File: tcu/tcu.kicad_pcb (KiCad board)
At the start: 2 copper layers, 52 parts, among them CON1 USB-MICRO-B, K1 SPDT_RELAY, K2 SPDT_RELAY, K3 SPDT_RELAY, P1 CONN_01X08, P2 CONN_02X03, P3 NRF24L01+, P4 ESP8266, Q1 E_NMOS, Q2 E_NMOS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

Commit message: further work on layout
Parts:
- D10: moved to B.Cu
- moved D10 108.0 mm to (68.1, 74.1)
- moved Q4 105.7 mm to (70.7, 60.1)
- moved R13 101.9 mm to (71.9, 65.2), turned to 180 degrees
- moved P4 99.3 mm to (163.3, 105.9), turned to 180 degrees
- moved P3 97.5 mm to (163.6, 84.3), turned to 180 degrees
- moved BR1 84.3 mm to (104.1, 39.4)
- moved BR3 84.3 mm to (134.6, 39.4)
- moved D1 84.3 mm to (149.9, 39.4)
- moved D3 84.3 mm to (88.9, 39.4)
- moved D5 84.3 mm to (88.9, 52.1)
- moved D6 84.3 mm to (149.9, 52.1)
- moved K1 84.3 mm to (111.8, 44.5)
- moved K2 84.3 mm to (81.3, 44.5)
- moved K3 84.3 mm to (142.2, 44.5)
- moved Q2 84.3 mm to (88.9, 47.0)
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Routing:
- net GND: track 0.00 -> 346.9 mm
- net Net-(C1-Pad1): track 0.00 -> 128.1 mm
- net Net-(BR2-Pad1): track 0.00 -> 60.3 mm
- net Net-(BR3-Pad2): track 0.00 -> 56.1 mm
- net VCC: track 0.00 -> 55.8 mm, vias 0 -> 1
- net Net-(BR3-Pad1): track 0.00 -> 37.9 mm
- net Net-(BR1-Pad1): track 0.00 -> 32.8 mm
- net Net-(BR1-Pad2): track 0.00 -> 30.7 mm
- net /MOSI: track 0.00 -> 18.2 mm, vias 0 -> 1
- net Net-(BR2-Pad2): track 18.9 -> 35.8 mm
- net Net-(D8-Pad2): track 0.00 -> 14.8 mm
- net /MISO: track 0.00 -> 9.08 mm
- net Net-(C4-Pad1): track 0.00 -> 8.67 mm
- net /SCK: track 0.00 -> 8.35 mm
- net Net-(C5-Pad1): track 0.00 -> 8.25 mm
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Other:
- net class power added: clearance 0.254, trace_width 0.6096, via_dia 0.889, via_drill 0.635

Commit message: squeezing in
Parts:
- moved F1 61.8 mm to (73.4, 75.2)
- moved CON1 60.8 mm to (77.0, 78.7)
- moved R1 60.8 mm to (77.0, 75.4)
- moved R2 60.8 mm to (78.7, 75.4)
- moved D7 58.4 mm to (75.4, 71.4), turned to 180 degrees
- moved P3 56.5 mm to (108.0, 74.2), turned to 0 degrees
- moved P4 52.7 mm to (116.6, 81.5), turned to 0 degrees
- moved C4 36.6 mm to (93.0, 64.8), turned to 90 degrees
- moved X1 35.7 mm to (96.3, 66.8), turned to 270 degrees
- moved U2 32.2 mm to (85.3, 66.5), turned to 90 degrees
- moved C6 31.4 mm to (76.5, 68.6), turned to 0 degrees
- moved C5 30.9 mm to (93.0, 69.1), turned to 270 degrees
- moved Q4 27.7 mm to (66.0, 87.4), turned to 180 degrees
- moved R10 23.4 mm to (93.0, 74.9), turned to 270 degrees
- moved R13 20.3 mm to (66.8, 84.8)
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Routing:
- net VCC: track 55.8 -> 177.4 mm, vias 1 -> 5
- net /RESET: track 6.77 -> 27.5 mm
- net GND: track 346.9 -> 361.2 mm, vias 0 -> 5
- net /D-: track 0.00 -> 10.9 mm, vias 0 -> 2
- net /D+: track 0.00 -> 9.58 mm, vias 0 -> 2
- net Net-(C1-Pad1): track 128.1 -> 119.7 mm
- net Net-(D10-Pad2): track 0.00 -> 7.50 mm, vias 0 -> 1
- net Net-(D10-Pad1): track 0.00 -> 2.70 mm, vias 0 -> 1
- net /MOSI: track 18.2 -> 20.0 mm, vias 1 -> 3
- net /UVCC: track 5.30 -> 7.02 mm
- net Net-(D7-Pad1): track 3.84 -> 5.42 mm
- net /SCK: track 8.35 -> 6.82 mm
- net /MISO: track 9.08 -> 7.55 mm
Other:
- net class Default: clearance 0.254 -> 0.1778
- net class power: clearance 0.254 -> 0.1778
- rule trace_clearance: 0.254 -> 0.1778

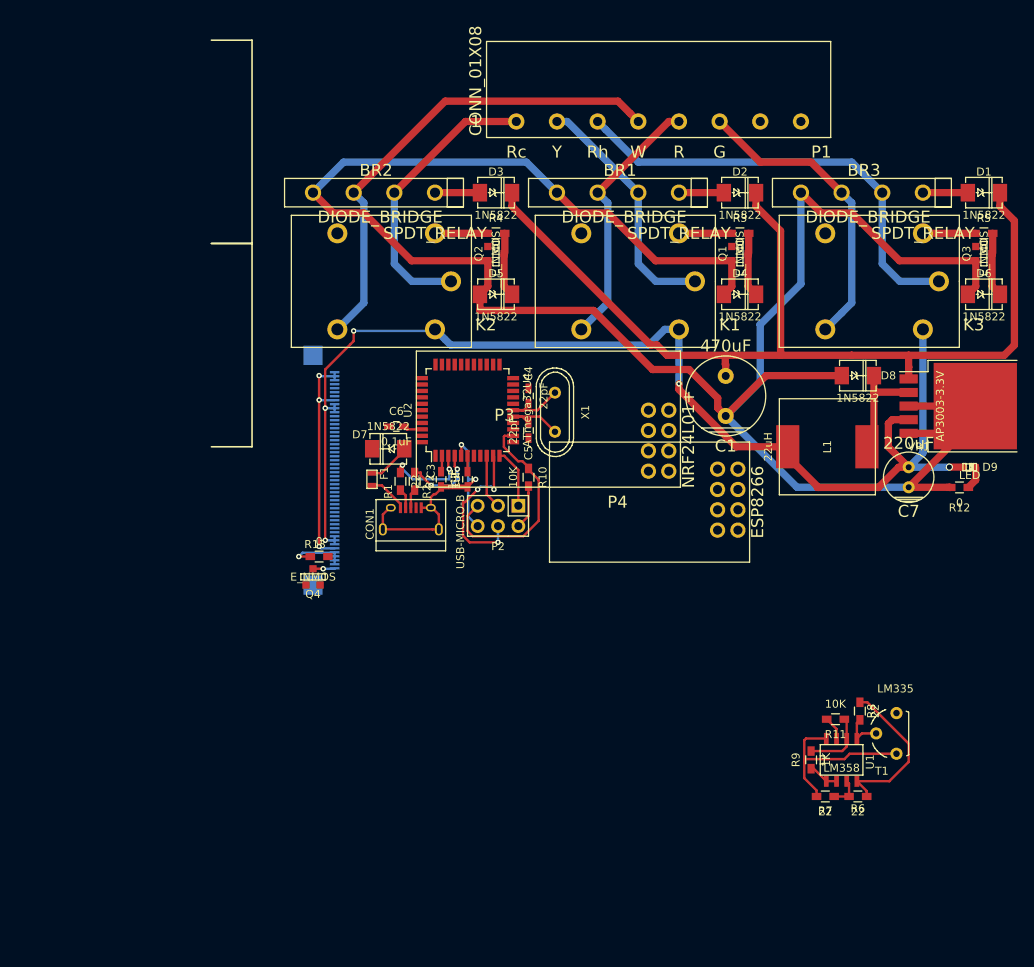
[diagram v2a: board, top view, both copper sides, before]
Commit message: moved left and right relay up
everything should fit vertically behind screen
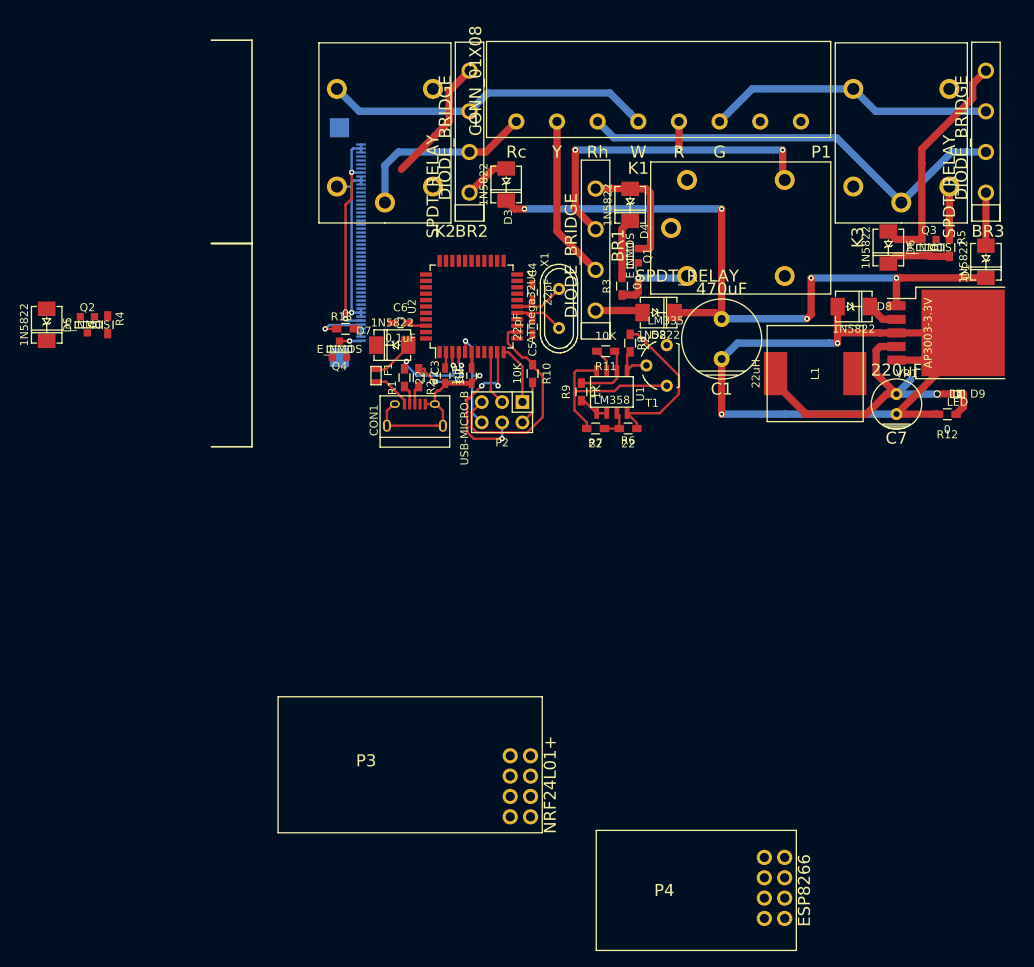
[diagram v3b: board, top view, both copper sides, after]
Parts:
- moved D5 56.3 mm to (32.8, 55.9), turned to 270 degrees
- moved R11 54.2 mm to (102.6, 59.2)
- moved R6 54.2 mm to (105.4, 68.8)
- moved R7 54.2 mm to (101.3, 68.8)
- moved R8 54.2 mm to (105.7, 58.2)
- moved R9 54.2 mm to (99.6, 64.3)
- moved U1 54.2 mm to (103.4, 64.3)
- moved T1 54.2 mm to (110.2, 61.0)
- moved Q2 51.8 mm to (37.8, 55.9), turned to 0 degrees
- moved R4 49.8 mm to (40.4, 55.9), turned to 270 degrees
- moved P4 48.9 mm to (122.4, 130.0)
- moved P3 46.5 mm to (90.7, 117.3)
- moved Q4 28.6 mm to (69.3, 58.9)
- moved R13 28.6 mm to (70.1, 56.4)
- moved D10 28.6 mm to (71.4, 45.6)
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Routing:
- net GND: track 361.2 -> 238.8 mm, vias 5 -> 6
- net VCC: track 177.4 -> 86.4 mm, vias 5 -> 2
- net Net-(C1-Pad1): track 119.7 -> 88.6 mm, vias 0 -> 5
- net Net-(BR2-Pad1): track 60.3 -> 41.2 mm
- net Net-(BR2-Pad2): track 35.8 -> 23.3 mm
- net Net-(BR1-Pad1): track 32.8 -> 44.3 mm, vias 0 -> 3
- net Net-(BR1-Pad2): track 30.7 -> 20.5 mm
- net Net-(D5-Pad2): track 8.07 -> 0.00 mm
- net Net-(D8-Pad2): track 14.8 -> 7.31 mm
- net Net-(K2-Pad5): track 6.52 -> 0.72 mm
- net Net-(K1-Pad5): track 6.52 -> 10.2 mm, vias 0 -> 1
- net Net-(BR3-Pad1): track 37.9 -> 36.1 mm
- net Net-(BR3-Pad3): track 5.61 -> 6.63 mm
- net Net-(BR3-Pad2): track 56.1 -> 55.3 mm
- net Net-(D4-Pad2): track 8.07 -> 7.47 mm

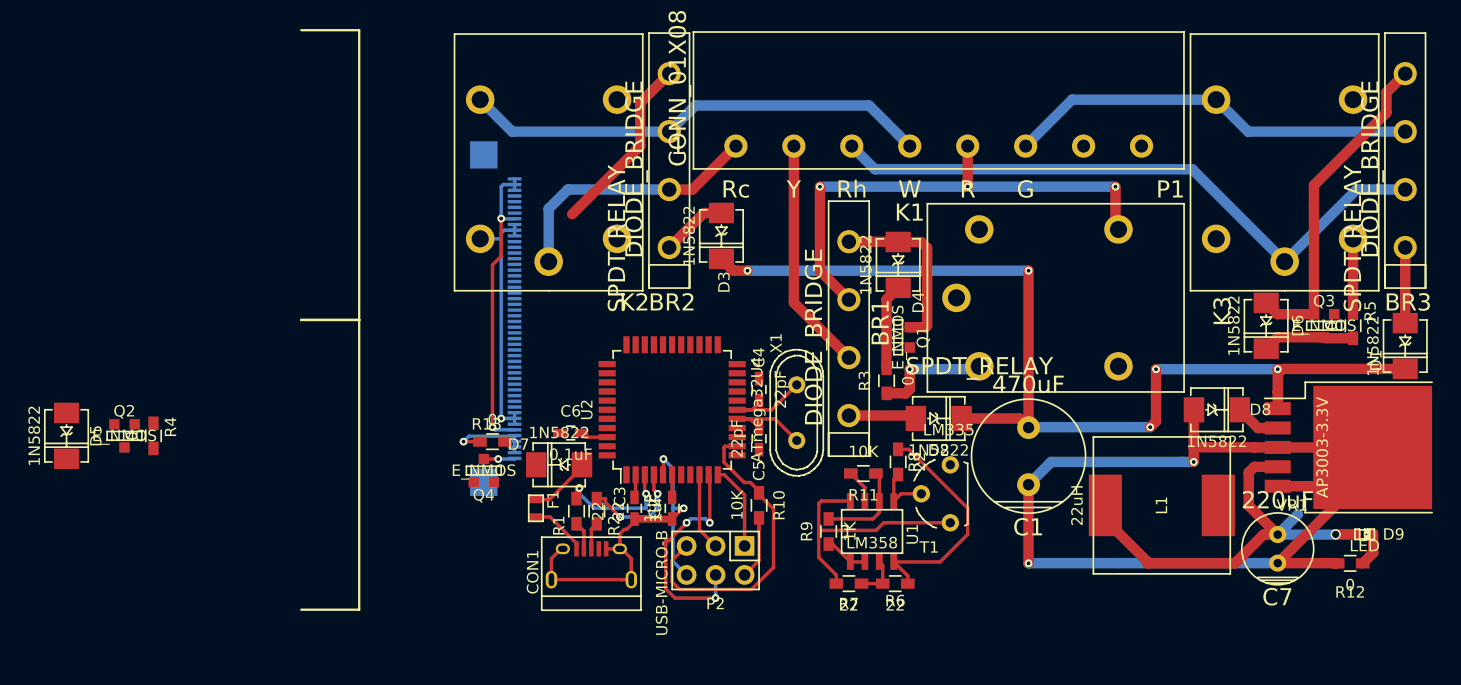
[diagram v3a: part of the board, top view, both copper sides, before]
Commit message: touchscreen routed
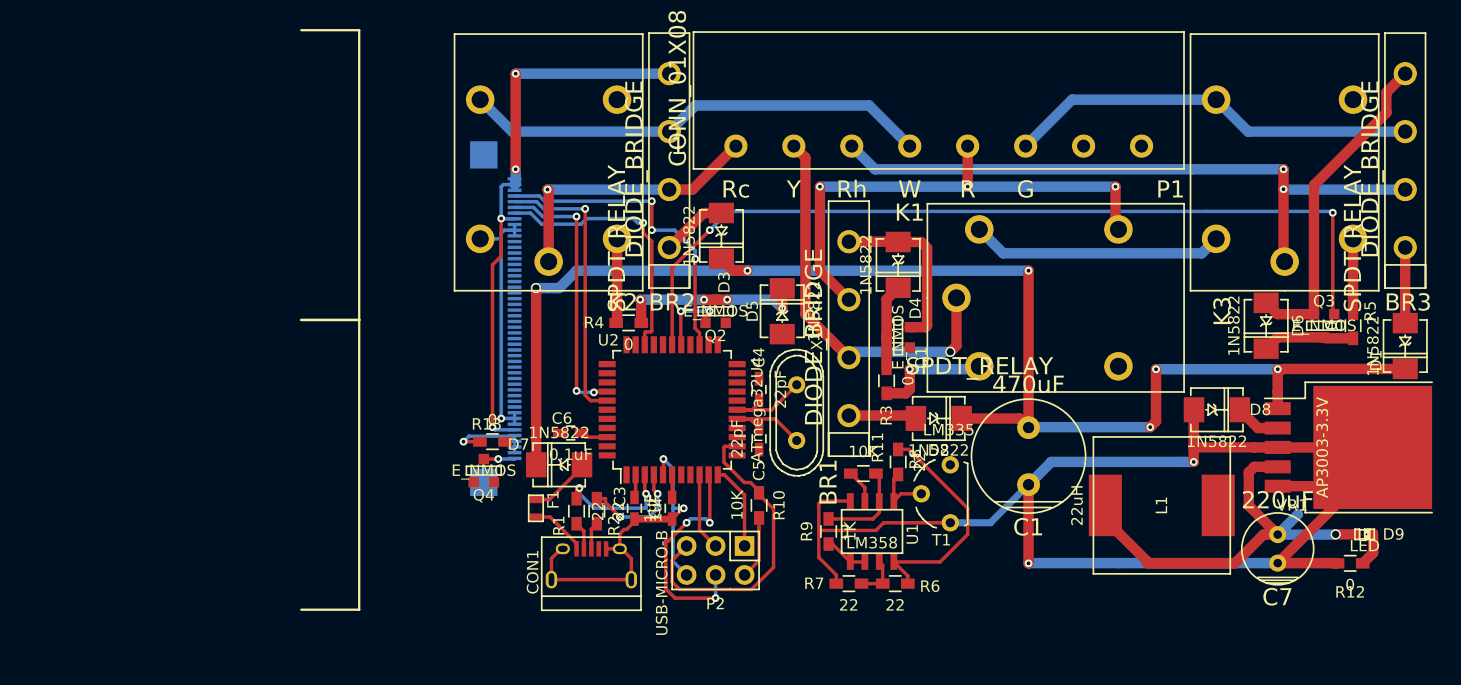
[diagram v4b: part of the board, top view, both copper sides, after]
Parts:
- moved D5 63.7 mm to (95.5, 45.0), turned to 90 degrees
- moved Q2 53.0 mm to (89.7, 45.0), turned to 180 degrees
- moved R4 42.8 mm to (82.0, 46.0), turned to 0 degrees
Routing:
- net /RELAY3: track 0.00 -> 75.7 mm, vias 0 -> 2
- net Net-(C1-Pad1): track 88.6 -> 123.3 mm, vias 5 -> 6
- net /Y-: track 0.00 -> 27.7 mm, vias 0 -> 3
- net /X-: track 0.00 -> 24.9 mm, vias 0 -> 1
- net /Y+: track 0.00 -> 23.8 mm, vias 0 -> 3
- net /X+: track 0.00 -> 23.6 mm, vias 0 -> 1
- net VCC: track 86.4 -> 108.6 mm
- net Net-(D5-Pad2): track 0.00 -> 16.6 mm, vias 0 -> 4
- net GND: track 238.8 -> 254.4 mm, vias 6 -> 8
- net Net-(BR1-Pad2): track 20.5 -> 34.6 mm, vias 0 -> 1
- net Net-(K2-Pad5): track 0.72 -> 7.40 mm
- net /RELAY1: track 0.00 -> 6.67 mm, vias 0 -> 2
- net Net-(BR3-Pad2): track 55.3 -> 57.5 mm, vias 0 -> 2
- net Net-(BR2-Pad2): track 23.3 -> 24.4 mm, vias 0 -> 1

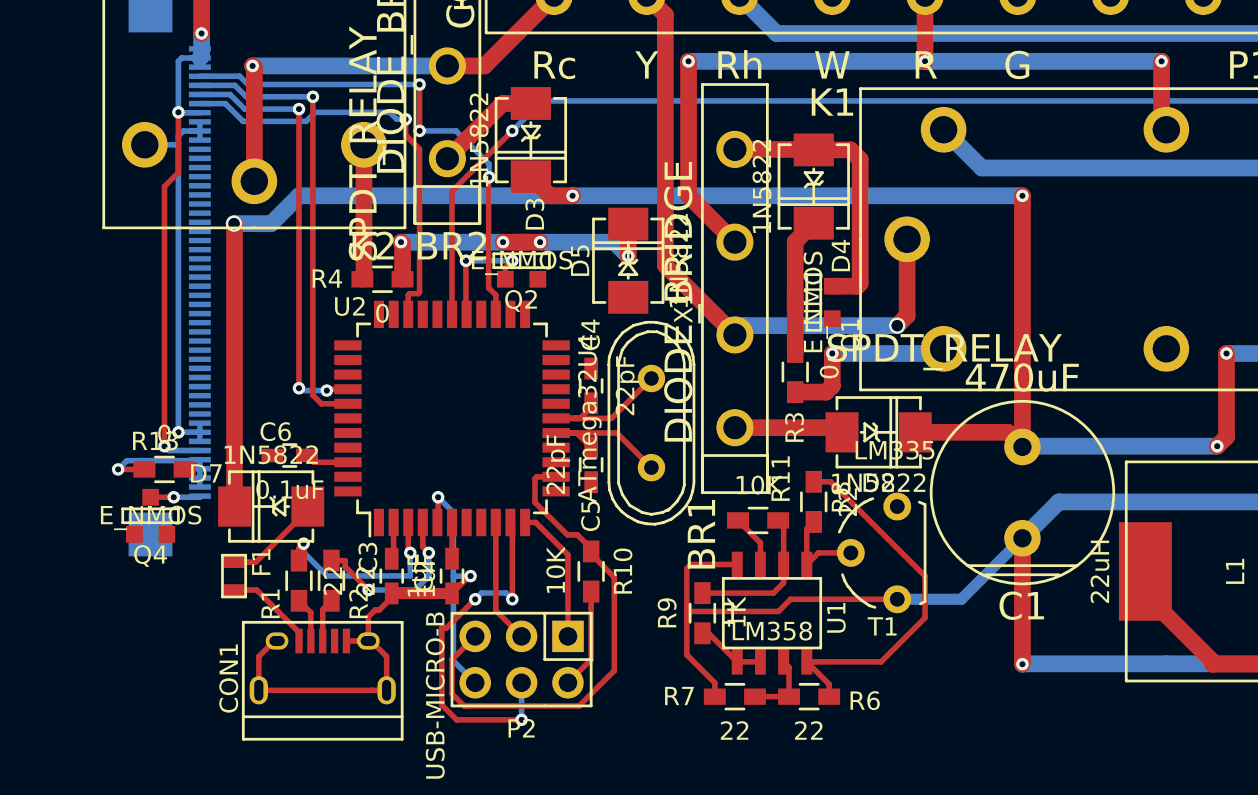
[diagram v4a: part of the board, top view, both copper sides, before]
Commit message: almost done routing lcd
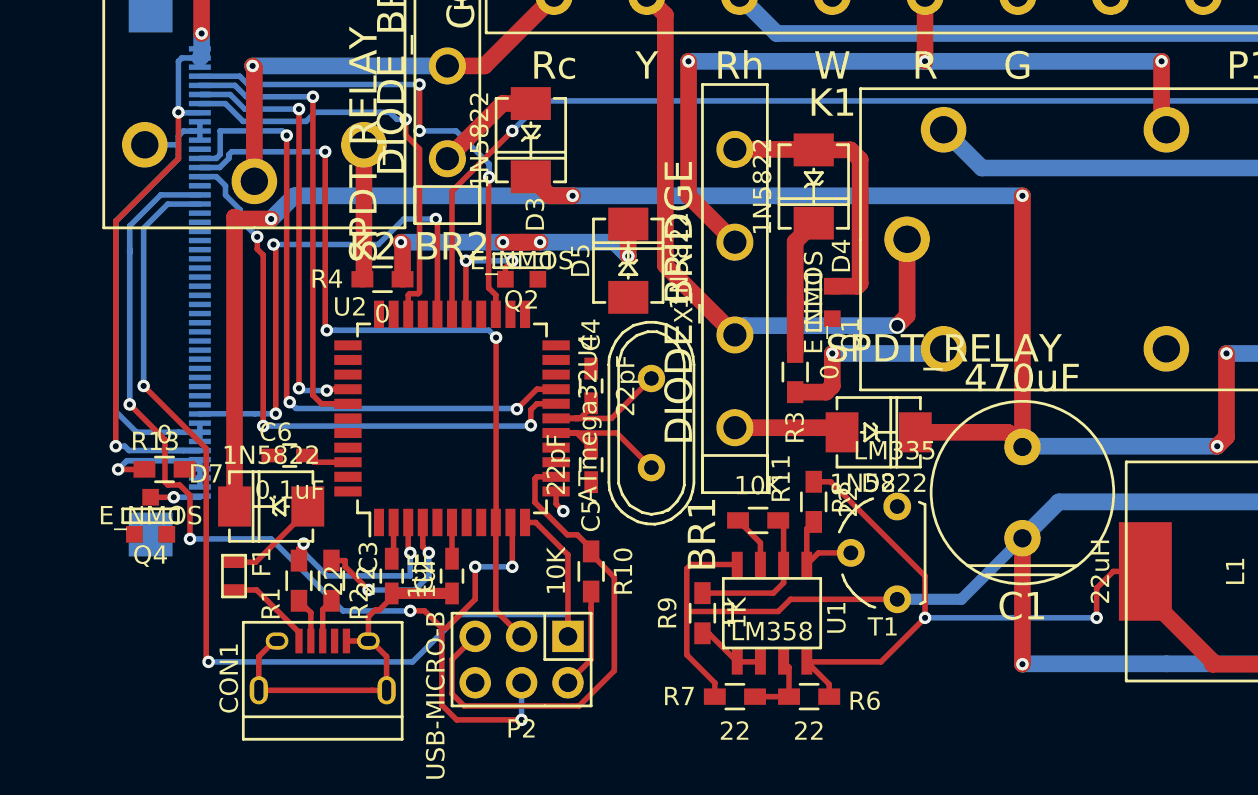
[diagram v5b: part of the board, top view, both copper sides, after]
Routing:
- net /MISO: track 7.55 -> 58.3 mm, vias 0 -> 2
- net /MOSI: track 20.0 -> 59.2 mm, vias 3 -> 6
- net /SCK: track 6.82 -> 43.6 mm, vias 0 -> 3
- net /LCD_CS: track 0.00 -> 36.1 mm, vias 0 -> 3
- net /D/C: track 0.00 -> 32.7 mm, vias 0 -> 3
- net /LCD_RESET: track 0.00 -> 28.2 mm, vias 0 -> 3
- net VCC: track 108.6 -> 126.8 mm, vias 2 -> 3
- net GND: track 254.4 -> 245.2 mm, vias 8 -> 6
- net /BACKLIGHT: track 0.00 -> 1.24 mm, vias 0 -> 1
